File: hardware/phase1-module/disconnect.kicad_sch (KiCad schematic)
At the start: 0 parts

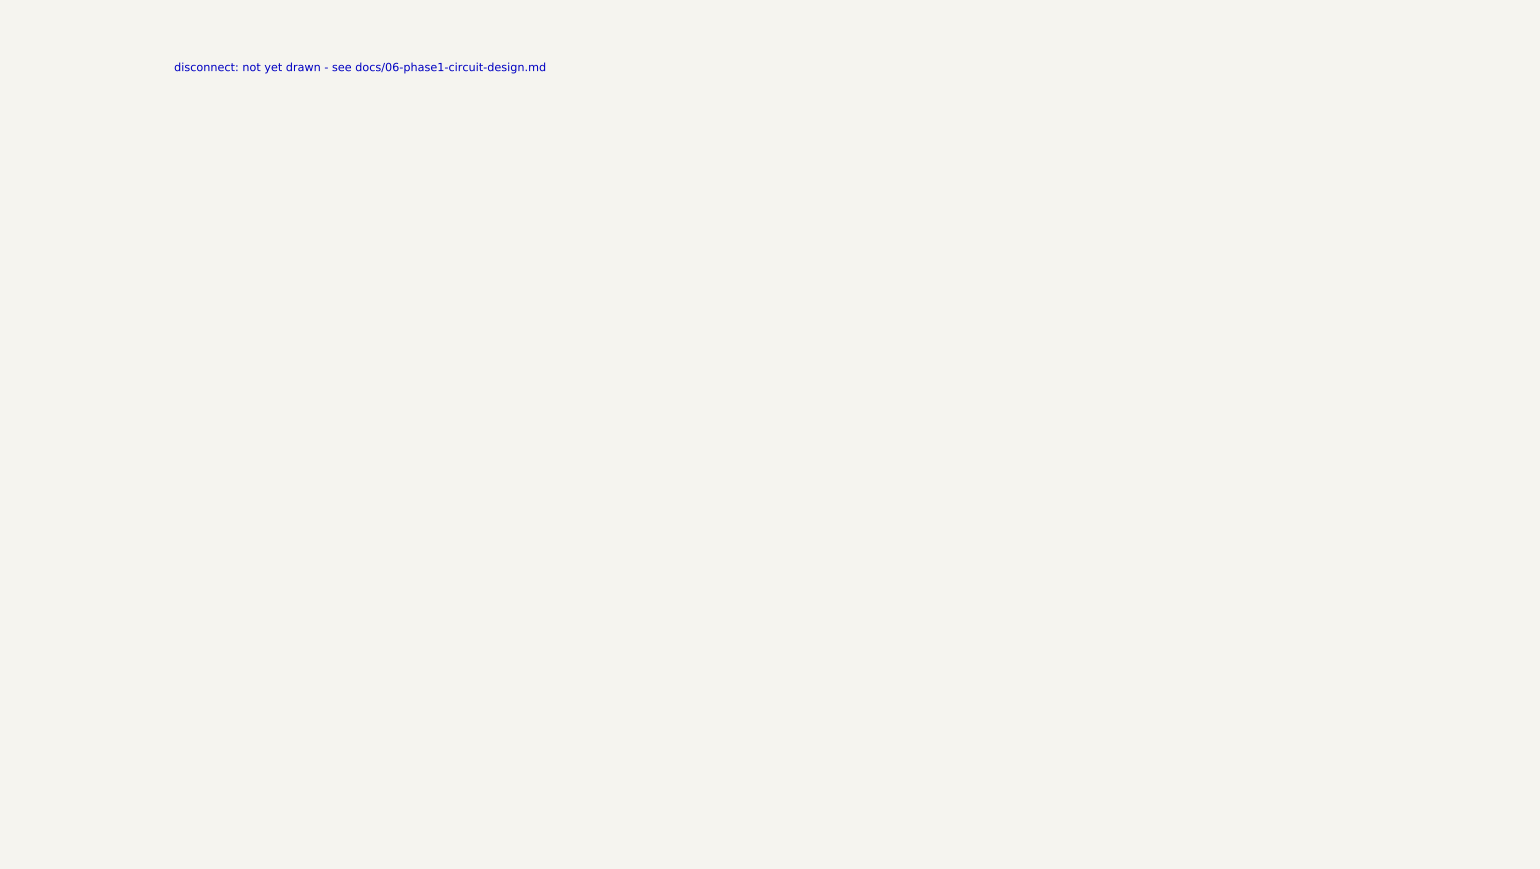
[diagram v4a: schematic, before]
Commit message: Complete Phase-1 schematic: all six remaining sheets, netlist-verified
- power-stage: LM5145 @350kHz (RT 28.7K per ds eq.3), RDS(on) valley
  ILIM 365R->SW, UVLO divider, EN kill chain (NOT(HW_EN) OR PS_OFF via
  Q5/Q6 + diode-OR), Type-III comp starting values, SYNCIN as DEM/FPWM
- sensing: 2m shunt, INA240A3 -> CC loop, INA228 telemetry, /8 divider,
  NT1 single AGND-PGND tie
- disconnect: back-to-back FETs + LTC7004, INP = OUT_REQ AND NOT(kill)
  AND NOT(OVP); TLV7011 + Q9 trips at 22.25V
- aux-rails: LMR36015 (5.016V) -> NCP1117 3V3
- mcu-can: STM32G431CBT6 fully pinned; I2C moved to I2C2/PA8-PA9 (PB8
  is the BOOT0 strap - pullup there would boot the ROM loader), BOOT0
  strapped low, OUT_REQ on PB14 (PB4 NJTRST reset pull-up), 8MHz
  crystal for CAN, TCAN1042 (VCC 5V, VIO 3V3)
- io: fused input + SMBJ33A TVS, output, backplane header, fan switch
  (1N4148W flyback orientation corrected: pin 1 = cathode)
- checker: duplicate-ref detection + global/local split-net detection;
  caught duplicate C62 and the LMR36015 FB-pin placement collision

Co-Authored-By: Claude Fable 5 <noreply@anthropic.com>
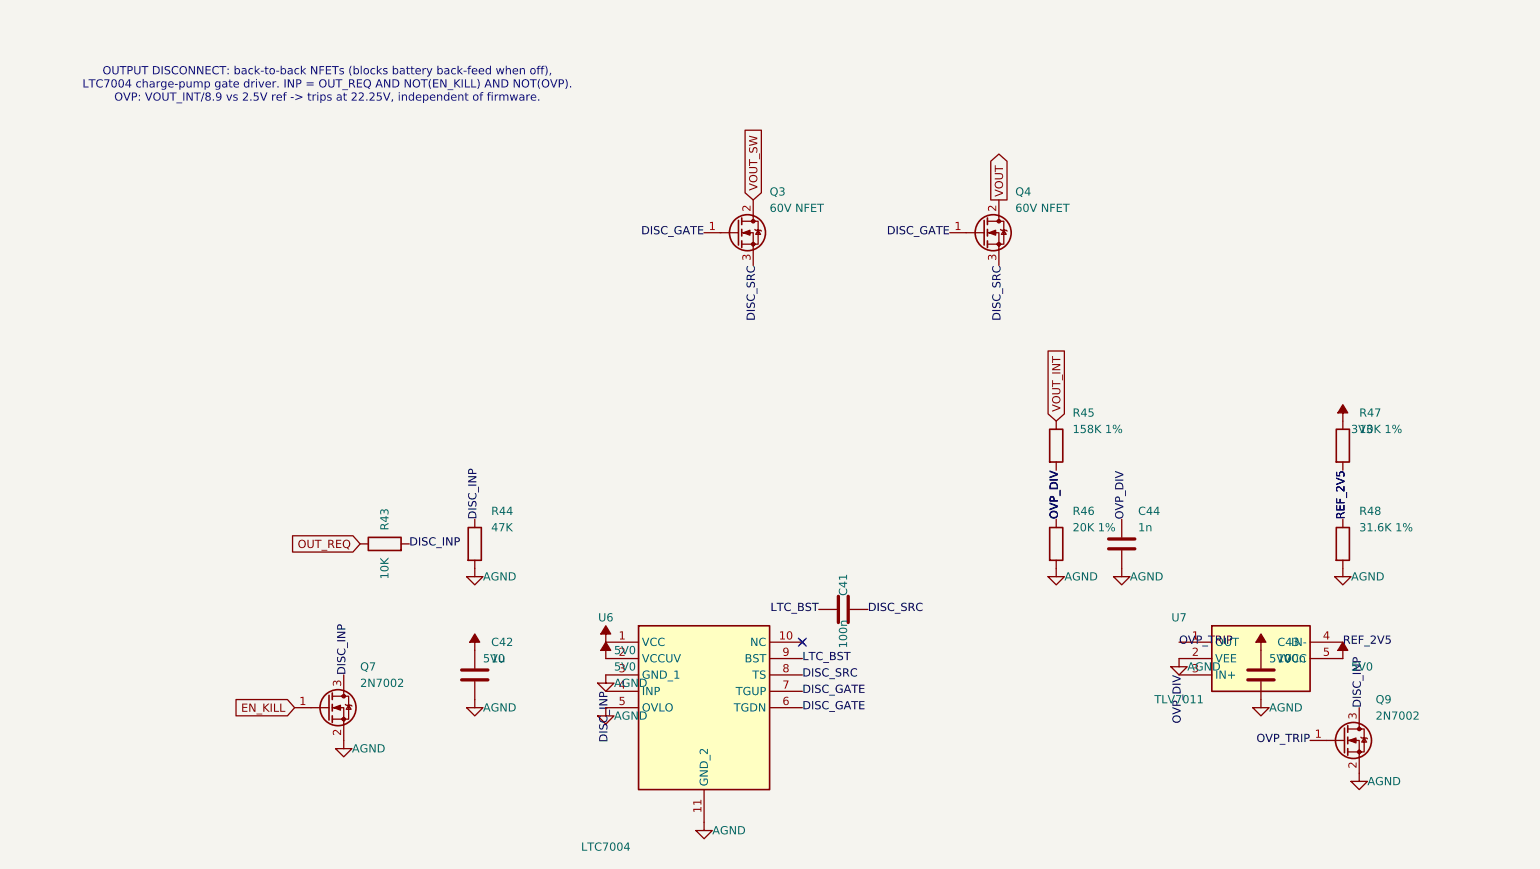
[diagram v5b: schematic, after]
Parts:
- added C41, C43: 100n, Capacitor_SMD:C_0402_1005Metric, symbol Device:C
- added C42: 1u, Capacitor_SMD:C_0402_1005Metric, symbol Device:C
- added C44: 1n, Capacitor_SMD:C_0402_1005Metric, symbol Device:C
- added Q3, Q4: 60V NFET, labbench:PowerFET_5x6, symbol Device:Q_NMOS_GDS
- added Q7, Q9: 2N7002, Package_TO_SOT_SMD:SOT-23, symbol Transistor_FET:2N7002
- added R43: 10K, Resistor_SMD:R_0402_1005Metric, symbol Device:R
- added R44: 47K, Resistor_SMD:R_0402_1005Metric, symbol Device:R
- added R45: 158K 1%, Resistor_SMD:R_0402_1005Metric, symbol Device:R
- added R46: 20K 1%, Resistor_SMD:R_0402_1005Metric, symbol Device:R
- added R47: 10K 1%, Resistor_SMD:R_0402_1005Metric, symbol Device:R
- added R48: 31.6K 1%, Resistor_SMD:R_0402_1005Metric, symbol Device:R
- added U6: LTC7004, Package_SO:MSOP-10-1EP_3x3mm_P0.5mm_EP1.68x1.88mm_ThermalVias, symbol labbench:LTC7004EMSE#TRPBF
- added U7: TLV7011, Package_TO_SOT_SMD:SOT-23-5, symbol labbench:TLV7011DBVR
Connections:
- new net 3V3: R47.1
- new net 5V0: C42.1, C43.1, U6.1 (VCC), U6.2 (VCCUV), U7.5 (VCC)
- new net AGND: C42.2, C43.2, C44.2, Q7.2 (S), Q9.2 (S), R44.2, R46.2, R48.2, U6.11 (GND_2), U6.3 (GND_1), U6.5 (OVLO), U7.2 (VEE)
- new net DISC_GATE: Q3.1 (G), Q4.1 (G), U6.6 (TGDN), U6.7 (TGUP)
- new net DISC_INP: Q7.3 (D), Q9.3 (D), R43.2, R44.1, U6.4 (INP)
- new net DISC_SRC: C41.2, Q3.3 (S), Q4.3 (S), U6.8 (TS)
- new net EN_KILL: Q7.1 (G)
- new net LTC_BST: C41.1, U6.9 (BST)
- new net OUT_REQ: R43.1
- new net OVP_DIV: C44.1, R45.2, R46.1, U7.3 (IN+)
- new net OVP_TRIP: Q9.1 (G), U7.1 (OUT)
- new net REF_2V5: R47.2, R48.1, U7.4 (IN-)
- new net VOUT: Q4.2 (D)
- new net VOUT_INT: R45.1
- new net VOUT_SW: Q3.2 (D)
- no-connect marks 0 -> 1
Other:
- note added: "OUTPUT DISCONNECT: back-to-back NFETs (blocks battery back-feed when off), LTC7004 charge-pump gate driver. INP = OUT_REQ AND NOT(EN_KILL) AND NOT(OVP). OVP: VOUT_INT/8.9 vs 2.5V ref -> trips at 22.25V, independent of firmware."
- note removed: "disconnect: not yet drawn - see docs/06-phase1-circuit-design.md"

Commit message: Footprint pass: labbench.pretty library, all 137 components verified
- build_fplib.py: merges vetted vendor footprints (LM5145 RGY0020B,
  LMR36015 RNX, DAC80502 WSON-10 no-EP) and generates PowerFET_SON5x6_GDS
  from the TI Q5A land pattern (CSD18563Q5A SLPS444C) with pads renumbered
  1=G/2=D/3=S to match the generic NMOS symbol; writes fp-lib-table.
- check_footprints.py: every component must have a resolvable footprint and
  every netted pin a matching pad (caught a wrong official VSSOP-8 name).
- gen_phase1.py: passives 0402->0603 (hand assembly); DAC80502 vendor fp
  (DRX has no exposed pad); L1 = Coilcraft XAL1350-103ME on official fp;
  net-tie fp; crystal -> Crystal_GND24 with grounded shield pads; bulk cap
  banks expanded to one component per physical cap (C75-C81); R27 preload
  1W -> 2512.
- PARTS-TO-DOWNLOAD.md section D: new orderables for the footprint pass.

check_netlist + check_footprints: all OK (137 components).

Co-Authored-By: Claude Fable 5 <noreply@anthropic.com>
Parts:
- C41, C42, C43, C44: footprint Capacitor_SMD:C_0402_1005Metric -> Capacitor_SMD:C_0603_1608Metric
- Q3, Q4: footprint labbench:PowerFET_5x6 -> labbench:PowerFET_SON5x6_GDS
- R43, R44, R45, R46, R47, R48: footprint Resistor_SMD:R_0402_1005Metric -> Resistor_SMD:R_0603_1608Metric

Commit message: PCB placement v1 + kicad-happy audit fixes
gen_board.py: netlist-driven board generator (120x80 4-layer) — placement
table for all 137 components, split In1 ground plane (PGND/AGND star at
NT1, AGND pocket under the LTC7004 cluster), In2 5V0/3V3 distribution,
9 F.Cu power pours with straddled cap banks, mechanical checks (pad-in-pour
assertions, courtyard overlap/edge detection). run_drc.py wraps pcbnew
WriteDRCReport (KiCad 7 has no CLI drc).

Audit (kicad-happy analyzers: schematic+PCB+cross+EMC+thermal) fixes:
- R31 100R -> 1K: INA240 rails at ~4.8V on the 5V rail during OC transients;
  PA1 is TT_a (3.6V) — 100R allowed ~12mA clamp injection vs 5mA abs max
- C43 moved to decouple U7 (was 21mm away), C50/C51 tight to U8 VIN
  (hot-loop), SW pour trimmed north (radiating area), 3 fiducials added,
  H2 courtyard off the board edge

Co-Authored-By: Claude Fable 5 <noreply@anthropic.com>
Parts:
- U6: footprint Package_SO:MSOP-10-1EP_3x3mm_P0.5mm_EP1.68x1.88mm_ThermalVias -> Package_SO:MSOP-10-1EP_3x3mm_P0.5mm_EP1.68x1.88mm
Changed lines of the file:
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@@
     (property "Reference" "U6" (at 76.2 123.19 0) (effects (font (size 1.27 1.27))))
     (property "Value" "LTC7004" (at 76.2 158.75 0) (effects (font (size 1.27 1.27))))
-    (property "Footprint" "Package_SO:MSOP-10-1EP_3x3mm_P0.5mm_EP1.68x1.88mm_ThermalVias" (at 76.2 127.0 0) (effects (font (size 1.27 1.27)) hide))
+    (property "Footprint" "Package_SO:MSOP-10-1EP_3x3mm_P0.5mm_EP1.68x1.88mm" (at 76.2 127.0 0) (effects (font (size 1.27 1.27)) hide))
     (property "Datasheet" "~" (at 76.2 127.0 0) (effects (font (size 1.27 1.27)) hide))
     (pin "1")

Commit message: Factor shared sheets + checkers into hardware/common for Phase-2 reuse
- hardware/common/kicad_gen.py (moved from phase1 tools; project lib dirs
  now registered via add_lib_dir so both phases share one library)
- hardware/common/sheets_common.py: control-core, sensing, disconnect,
  aux-rails, mcu-can extracted verbatim as parameterized builders (docs/05:
  control core reused as a hierarchical block); phase-specific values are
  parameters, refs and topology unchanged
- hardware/common/netcheck.py: netlist/footprint assertion logic shared;
  per-project check_*.py become thin CLI wrappers
- gen_phase1.py passes Phase-1 parameter sets; power-stage and io stay local
- Verified: regenerated Phase-1 netlist topology IDENTICAL to pre-refactor
  (100 nets), check_netlist all nets OK, check_footprints 137 components OK

Co-Authored-By: Claude Fable 5 <noreply@anthropic.com>
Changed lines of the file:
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@@
   (global_label "VOUT_SW" (shape input) (at 99.06 58.42 90) (fields_autoplaced) (effects (font (size 1.27 1.27))))
   (label "DISC_SRC" (at 99.06 68.58 270) (effects (font (size 1.27 1.27))))
+  (label "DISC_GATE" (at 91.44 63.5 180) (effects (font (size 1.27 1.27))))
+  (global_label "VOUT" (shape output) (at 137.16 58.42 90) (fields_autoplaced) (effects (font (size 1.27 1.27))))
   (label "DISC_SRC" (at 137.16 68.58 270) (effects (font (size 1.27 1.27))))
-  (global_label "VOUT" (shape output) (at 137.16 58.42 90) (fields_autoplaced) (effects (font (size 1.27 1.27))))
-  (label "DISC_GATE" (at 91.44 63.5 180) (effects (font (size 1.27 1.27))))
   (label "DISC_GATE" (at 129.54 63.5 180) (effects (font (size 1.27 1.27))))
   (no_connect (at 106.68 127.0))
@@
   (label "REF_2V5" (at 190.5 127.0 0) (effects (font (size 1.27 1.27))))
   (label "OVP_TRIP" (at 165.1 127.0 0) (effects (font (size 1.27 1.27))))
-  (label "OVP_TRIP" (at 185.42 142.24 180) (effects (font (size 1.27 1.27))))
-  (label "DISC_INP" (at 193.04 137.16 90) (effects (font (size 1.27 1.27))))
-  (text "OUTPUT DISCONNECT: back-to-back NFETs (blocks battery back-feed when off),\nLTC7004 charge-pump gate driver. INP = OUT_REQ AND NOT(EN_KILL) AND NOT(OVP).\nOVP: VOUT_INT/8.9 vs 2.5V ref -> trips at 22.25V, independent of firmware." (at 33.02 40.64 0) (effects (font (size 1.27 1.27))))
+  (label "OVP_TRIP" (at 200.66 142.24 180) (effects (font (size 1.27 1.27))))
+  (label "DISC_INP" (at 208.28 137.16 90) (effects (font (size 1.27 1.27))))
+  (text "OUTPUT DISCONNECT: back-to-back NFETs (blocks battery back-feed when off),\nLTC7004 charge-pump gate driver. INP = OUT_REQ AND NOT(EN_KILL) AND NOT(OVP).\nOVP: VOUT_INT/8.9 vs 2.5V ref -> trips at 22.25V, independent of firmware." (at 33.02 33.02 0) (effects (font (size 1.27 1.27))))
   (symbol (lib_id "Device:Q_NMOS_GDS") (at 96.52 63.5 0) (unit 1)
     (in_bom yes) (on_board yes) (dnp no)
@@
     (instances (project "phase1-module" (path "/e63e39d7-6ac0-4ffa-9e5c-2b84c50a0001/e63e39d7-6ac0-4ffa-9e5c-2b84c50a0013" (reference "#PWR084") (unit 1))))
   )
-  (symbol (lib_id "Transistor_FET:2N7002") (at 190.5 142.24 0) (unit 1)
-    (in_bom yes) (on_board yes) (dnp no)
-    (property "Reference" "Q9" (at 195.57999999999998 135.89 0) (effects (font (size 1.27 1.27)) (justify left)))
-    (property "Value" "2N7002" (at 195.57999999999998 138.43 0) (effects (font (size 1.27 1.27)) (justify left)))
-    (property "Footprint" "Package_TO_SOT_SMD:SOT-23" (at 190.5 142.24 0) (effects (font (size 1.27 1.27)) hide))
-    (property "Datasheet" "~" (at 190.5 142.24 0) (effects (font (size 1.27 1.27)) hide))
+  (symbol (lib_id "Transistor_FET:2N7002") (at 205.74 142.24 0) (unit 1)
+    (in_bom yes) (on_board yes) (dnp no)
+    (property "Reference" "Q9" (at 210.82 135.89 0) (effects (font (size 1.27 1.27)) (justify left)))
+    (property "Value" "2N7002" (at 210.82 138.43 0) (effects (font (size 1.27 1.27)) (justify left)))
+    (property "Footprint" "Package_TO_SOT_SMD:SOT-23" (at 205.74 142.24 0) (effects (font (size 1.27 1.27)) hide))
+    (property "Datasheet" "~" (at 205.74 142.24 0) (effects (font (size 1.27 1.27)) hide))
     (pin "1")
     (pin "2")
@@
     (instances (project "phase1-module" (path "/e63e39d7-6ac0-4ffa-9e5c-2b84c50a0001/e63e39d7-6ac0-4ffa-9e5c-2b84c50a0013" (reference "Q9") (unit 1))))
   )
-  (symbol (lib_id "LB_PWR:AGND") (at 193.04 147.32 0) (unit 1)
-    (in_bom yes) (on_board yes) (dnp no)
-    (property "Reference" "#PWR085" (at 194.31 146.04999999999998 0) (effects (font (size 1.27 1.27)) (justify left) hide))
-    (property "Value" "AGND" (at 194.31 148.59 0) (effects (font (size 1.27 1.27)) (justify left)))
-    (property "Footprint" "" (at 193.04 147.32 0) (effects (font (size 1.27 1.27)) hide))
-    (property "Datasheet" "~" (at 193.04 147.32 0) (effects (font (size 1.27 1.27)) hide))
+  (symbol (lib_id "LB_PWR:AGND") (at 208.28 147.32 0) (unit 1)
+    (in_bom yes) (on_board yes) (dnp no)
+    (property "Reference" "#PWR085" (at 209.55 146.04999999999998 0) (effects (font (size 1.27 1.27)) (justify left) hide))
+    (property "Value" "AGND" (at 209.55 148.59 0) (effects (font (size 1.27 1.27)) (justify left)))
+    (property "Footprint" "" (at 208.28 147.32 0) (effects (font (size 1.27 1.27)) hide))
+    (property "Datasheet" "~" (at 208.28 147.32 0) (effects (font (size 1.27 1.27)) hide))
     (pin "1")
     (instances (project "phase1-module" (path "/e63e39d7-6ac0-4ffa-9e5c-2b84c50a0001/e63e39d7-6ac0-4ffa-9e5c-2b84c50a0013" (reference "#PWR085") (unit 1))))
